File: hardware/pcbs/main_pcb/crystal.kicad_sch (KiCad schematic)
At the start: 3 parts, among them Y1 Crystal_GND24

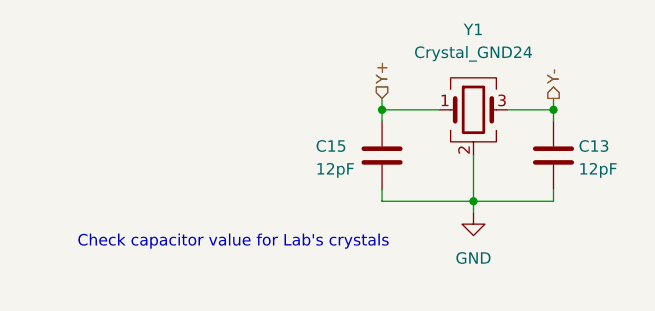
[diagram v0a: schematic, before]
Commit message: Maddie/main pcb schematic cleaning (#88)
* feat(main PCB): Reworks schematic

* feat(main PCB): Removes no longer used BL pin 01x02 header

* feat(main PCB): Fixes main PCB routing issue

* chore: Reworks main PCB schematic/PCB

* chore: Removes old csv file
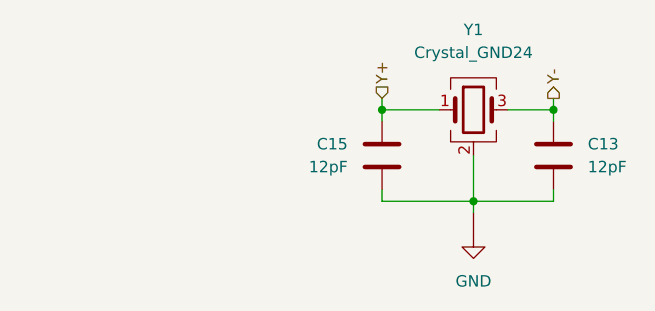
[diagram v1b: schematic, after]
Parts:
- C13, C15: symbol Device:C -> Lilybrary:Capacitor
- Y1: symbol Device:Crystal_GND24 -> Lilybrary:Crystal; private (none) -> KLC_S4.1
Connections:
- net GND renamed G
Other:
- note removed: "Check capacitor value for Lab's crystals"
- company: (none) -> Lily's Pad
- title: (none) -> Main PCB: Crystal
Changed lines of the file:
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@@
 	(generator_version "9.0")
 	(paper "A4")
-	(text "Check capacitor value for Lab's crystals\n"
-		(exclude_from_sim no)
-		(at 93.98 103.632 0)
-		(effects
-			(font
-				(size 1.27 1.27)
-			)
-		)
+	(title_block
+		(title "Main PCB: Crystal")
+		(date "2026-10-13")
+		(rev "v1.0")
+		(company "Lily's Pad")
 	)
 	(junction
@@
 	(wire
 		(pts
-			(xy 120.65 99.06) (xy 120.65 93.98)
+			(xy 120.65 93.98) (xy 120.65 99.06)
 		)
 		(stroke
@@
 	)
 	(symbol
-		(lib_id "Device:C")
+		(lib_id "Lilybrary:Capacitor")
 		(at 110.49 93.98 180)
 		(unit 1)
@@
 		(on_board yes)
 		(dnp no)
+		(fields_autoplaced yes)
 		(property "Reference" "C15"
-			(at 103.124 92.964 0)
-			(effects
-				(font
-					(size 1.27 1.27)
-				)
-				(justify right)
+			(at 106.68 92.7099 0)
+			(effects
+				(font
+					(size 1.27 1.27)
+				)
+				(justify left)
 			)
 		)
 		(property "Value" "12pF"
-			(at 103.124 95.504 0)
-			(effects
-				(font
-					(size 1.27 1.27)
-				)
-				(justify right)
+			(at 106.68 95.2499 0)
+			(effects
+				(font
+					(size 1.27 1.27)
+				)
+				(justify left)
 			)
 		)
 		(property "Footprint" "Lilibrary:Capacitor_0603"
-			(at 109.5248 90.17 0)
+			(at 110.49 93.98 0)
 			(effects
 				(font
@@
 			)
 		)
-		(property "Description" ""
+		(property "Description" "Unpolarized capacitor"
 			(at 110.49 93.98 0)
 			(effects
@@
 	)
 	(symbol
-		(lib_id "Device:C")
+		(lib_id "Lilybrary:Capacitor")
 		(at 129.54 93.98 180)
 		(unit 1)
@@
 		(on_board yes)
 		(dnp no)
+		(fields_autoplaced yes)
 		(property "Reference" "C13"
-			(at 132.334 92.964 0)
+			(at 133.35 92.7099 0)
 			(effects
 				(font
@@
 		)
 		(property "Value" "12pF"
-			(at 132.334 95.504 0)
+			(at 133.35 95.2499 0)
 			(effects
 				(font
@@
 		)
 		(property "Footprint" "Lilibrary:Capacitor_0603"
-			(at 128.5748 90.17 0)
+			(at 129.54 93.98 0)
 			(effects
 				(font
@@
 			)
 		)
-		(property "Description" ""
+		(property "Description" "Unpolarized capacitor"
 			(at 129.54 93.98 0)
 			(effects
@@
 	)
 	(symbol
-		(lib_id "power:GND")
-		(at 120.65 100.33 0)
+		(lib_id "Lilybrary:GND")
+		(at 120.65 102.87 0)
 		(unit 1)
 		(exclude_from_sim no)
-		(in_bom yes)
-		(on_board yes)
+		(in_bom no)
+		(on_board no)
 		(dnp no)
 		(fields_autoplaced yes)
 		(property "Reference" "#PWR017"
-			(at 120.65 106.68 0)
+			(at 120.65 109.22 0)
 			(effects
 				(font
@@
 		)
 		(property "Value" "GND"
-			(at 120.65 105.41 0)
+			(at 120.65 107.95 0)
 			(effects
 				(font
@@
 		)
 		(property "Footprint" ""
-			(at 120.65 100.33 0)
+			(at 120.65 102.87 0)
 			(effects
 				(font
@@
 		)
 		(property "Datasheet" ""
-			(at 120.65 100.33 0)
+			(at 120.65 102.87 0)
 			(effects
 				(font
@@
 		)
 		(property "Description" "Power symbol creates a global label with name \"GND\" , ground"
-			(at 120.65 100.33 0)
+			(at 120.65 102.87 0)
 			(effects
 				(font
@@
 	)
 	(symbol
-		(lib_id "Device:Crystal_GND24")
+		(lib_id "Lilybrary:Crystal")
 		(at 120.65 88.9 0)
 		(unit 1)
@@
 			)
 		)
-		(property "Description" ""
+		(property "Description" "Four pin crystal, GND on pins 2 and 4"
 			(at 120.65 88.9 0)
 			(effects
@@
 			(effects
 				(font
+					(size 1.27 1.27)
+				)
+				(hide yes)
+			)
+		)
+		(property private "KLC_S3.3" "The rectangle is not a symbol body but a graphical element"
+			(at 120.65 101.6 0)
+			(effects
+				(font
+					(size 1.27 1.27)
+				)
+				(hide yes)
+			)
+		)
+		(property private "KLC_S4.1" "Some pins are on 50mil grid to make the symbol small"
+			(at 120.65 104.14 0)
+			(effects
+				(font
